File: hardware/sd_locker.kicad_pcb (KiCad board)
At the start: 2 copper layers, 29.2 x 38.1 mm, 17 parts, among them J1 USB_OTG, J2 3V3, J3 5V, J4 SD_Card, Q1 Q_PMOS_GSD, SW1 SW_Push, U1 AP1117-33, U2 ATTINY85-20SU

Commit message: Unverified - fixing the SD locker PCB layout so that airwires are not needed for SD slot connection, adding proper CD wire, adding 0R resistor for easier "battery-powered SD locker" modding
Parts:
- added R5: 0, Resistors_SMD:R_0603_HandSoldering, F.Cu at (137.9, 99.7)
- J3: value 5V -> VIN
- moved R4 5.35 mm to (134.2, 95.9), turned to 180 degrees
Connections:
- J1 pad 1: VBUS -> Net-(J1-Pad1)
- J1 pad 2: (no net) -> Net-(J1-Pad2)
- J1 pad 3: (no net) -> Net-(J1-Pad3)
- J1 pad 4: (no net) -> Net-(J1-Pad4)
- J3 pad 2: +5V -> VBUS
- J4 pad : GND -> (no net)
- J4 pad 8: (no net) -> Net-(J4-Pad8)
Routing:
- net CD: track 3.11 -> 30.0 mm, vias 0 -> 2
- net CS: track 17.6 -> 39.3 mm, vias 0 -> 2
- net MISO: track 22.2 -> 7.16 mm, vias 2 -> 0
- net MOSI: track 13.3 -> 25.5 mm, vias 2 -> 0
- net VBUS: track 6.04 -> 17.5 mm
- net +5V: track 11.8 -> 7.10 mm
- net Net-(J1-Pad1): track 0.00 -> 2.61 mm
- net SCK: track 15.5 -> 14.0 mm, vias 2 -> 0
- net +3V3: track 41.1 -> 42.6 mm
- net GND: vias 0 -> 14
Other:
- board text added: "v2"

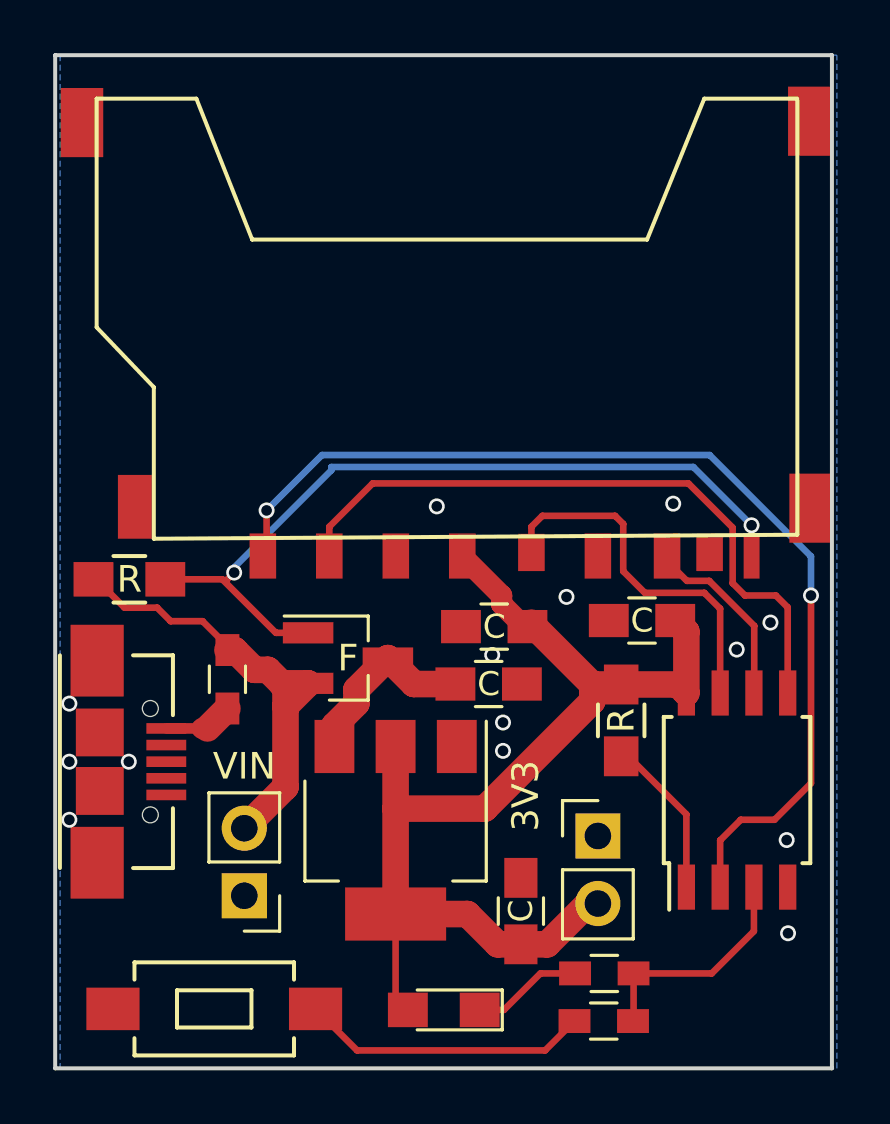
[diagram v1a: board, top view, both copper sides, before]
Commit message: Latest hardware version (v2) added
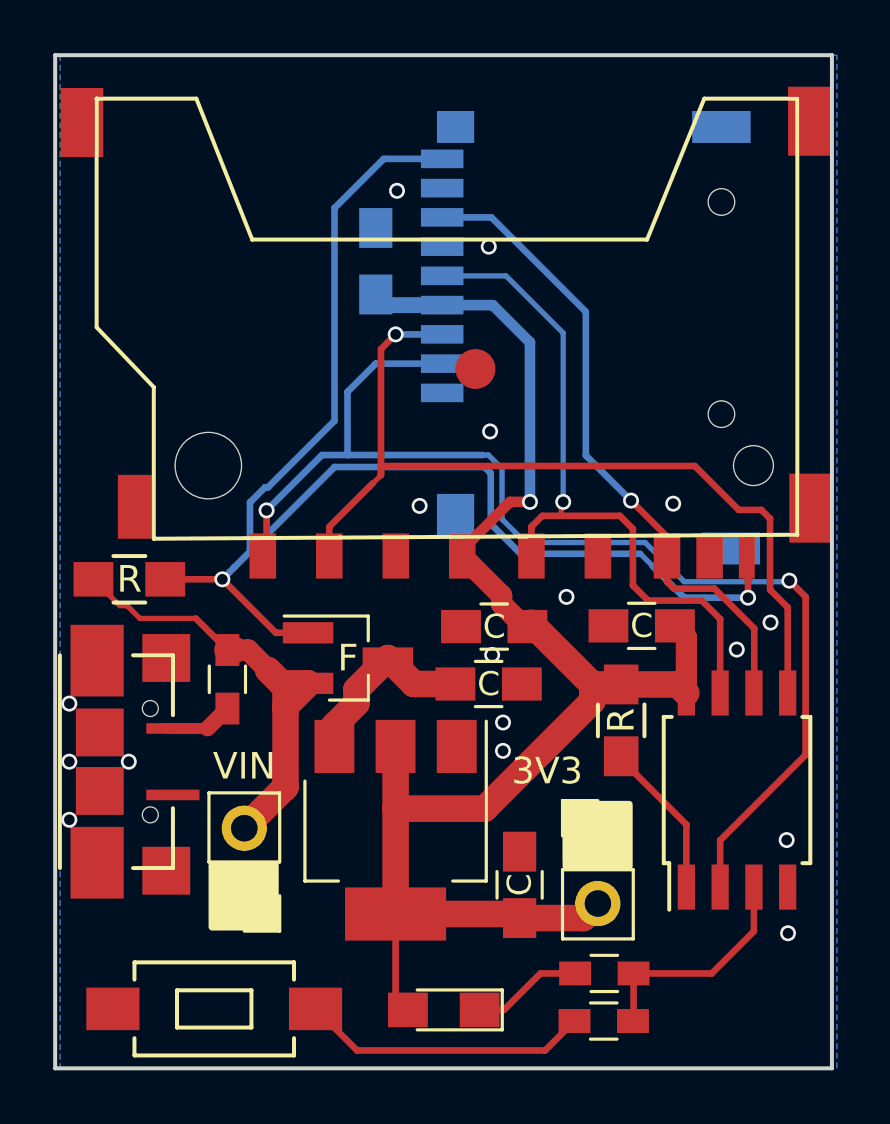
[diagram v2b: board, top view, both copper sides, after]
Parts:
- added C5: 100nF, sd_locker:C_0805_100nF_HandSoldering, B.Cu at (143.5, 84.0)
- added FID1: Fiducial, Fiducial:Fiducial_1.5mm_Mask3mm, F.Cu at (147.2, 88.0)
- added J5: Micro_SD_Card_Det, sd_locker:microSD-Receptacle-SelfEject, B.Cu at (146.0, 86.7)
- moved C3 0.99 mm to (148.9, 107.4)
- moved C2 0.20 mm to (153.5, 97.7)
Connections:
- J4 pad 8: Net-(J4-Pad8) -> (no net)
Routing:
- net CD: track 30.0 -> 51.6 mm
- net MISO: track 7.16 -> 25.3 mm, vias 0 -> 1
- net +3V3: track 42.6 -> 58.1 mm, vias 0 -> 1
- net SCK: track 14.0 -> 26.3 mm, vias 0 -> 1
- net MOSI: track 25.5 -> 34.0 mm, vias 0 -> 1
- net CS: track 39.3 -> 44.9 mm
- net Net-(J1-Pad1): track 2.61 -> 3.58 mm
- net VBUS: track 17.5 -> 18.0 mm
- net GND: vias 14 -> 17
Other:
- board text added: "(LED lit=locked ; LED unlit=unlocked) 5) press button to toggle status"
- board text added: "3) locker will boot for ~~3 seconds (LED will be lit) 4) once booted, card status will show"
- board text added: "How to use: 1) plug USB 2) plug SD card"
- board text added: "SD locker v2 by CRimier"
- board text added: "fast flash = connection problem"
- board text added: "for PERM lock, hold button while inserting SD card, LED will flash SOS"

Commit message: Adding a fiducial on the bottom layer
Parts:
- added FID2: Fiducial, Fiducial:Fiducial_1.5mm_Mask3mm, B.Cu at (134.0, 83.5)
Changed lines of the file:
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@@
     (tracks 194)
     (zones 0)
-    (modules 21)
+    (modules 22)
     (nets 15)
   )
@@
   )
   (setup
-    (last_trace_width 0.25)
+    (last_trace_width 0.2)
     (user_trace_width 0.2)
     (user_trace_width 0.4)
@@
     (add_net "Net-(D1-Pad1)")
     (add_net "Net-(J1-Pad1)")
+    (add_net "Net-(J4-Pad8)")
+    (add_net "Net-(J5-Pad1)")
+    (add_net "Net-(J5-Pad8)")
     (add_net "Net-(R1-Pad2)")
     (add_net "Net-(R2-Pad1)")
@@
     (add_net VBUS)
   )
+  (module Fiducial:Fiducial_1.5mm_Mask3mm (layer B.Cu)
+    (at 134 83.5)
+    (descr "Circular Fiducial, 1.5mm bare copper, 3mm soldermask opening")
+    (tags fiducial)
+    (attr smd)
+    (fp_text reference FID2 (at 0 2.4765) (layer B.SilkS) hide
+      (effects (font (size 1 1) (thickness 0.15)) (justify mirror))
+    )
+    (fp_text value Fiducial (at 0 -2.6035) (layer B.Fab)
+      (effects (font (size 1 1) (thickness 0.15)) (justify mirror))
+    )
+    (fp_circle (center 0 0) (end 1.75 0) (layer B.CrtYd) (width 0.05))
+    (fp_text user %R (at 0 0) (layer B.Fab)
+      (effects (font (size 0.4 0.4) (thickness 0.06)) (justify mirror))
+    )
+    (fp_circle (center 0 0) (end 1.5 0) (layer B.Fab) (width 0.1))
+    (pad "" smd circle (at 0 0) (size 1.5 1.5) (layers B.Cu B.Mask)
+      (solder_mask_margin 0.75) (clearance 0.75))
+  )
   (module sd_locker:microSD-Receptacle-SelfEject (layer B.Cu)

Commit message: Latest hardware revision, v3, wasn't uplaoded for a long time - fixed
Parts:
- added R6: 0, Resistor_SMD:R_0603_1608Metric_Pad1.05x0.95mm_HandSolder, F.Cu at (153.5, 102.7)
- R5: footprint Resistors_SMD:R_0603_HandSoldering -> Resistor_SMD:R_0603_1608Metric_Pad1.05x0.95mm_HandSolder
- moved R1 1.07 mm to (151.8, 101.7)
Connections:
- net Net-(R1-Pad2) renamed RST
- J4 pad 8: (no net) -> Net-(J4-Pad8)
- J5 pad 1: (no net) -> Net-(J5-Pad1)
- J5 pad 8: (no net) -> Net-(J5-Pad8)
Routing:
- net Net-(J4-Pad8): track 0.00 -> 18.3 mm, vias 0 -> 2
- net RST: track 5.94 -> 7.39 mm
- net GND: vias 17 -> 18
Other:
- board text added: "SD locker v3 by CRimier"
- board text added: "v3"
- board text removed: "SD locker v2 by CRimier"
- board text removed: "v2"
